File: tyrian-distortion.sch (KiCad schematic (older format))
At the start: 84 parts, among them J1 AudioJack2, J2 AudioJack2, J3 Barrel_Jack_Switch, J4 Conn_01x02_Female, SW1 SW_DPDT_x2, SW2 SW_3PDT, U1 TL072, U2 TL072, U3 TL072, U4 TL072

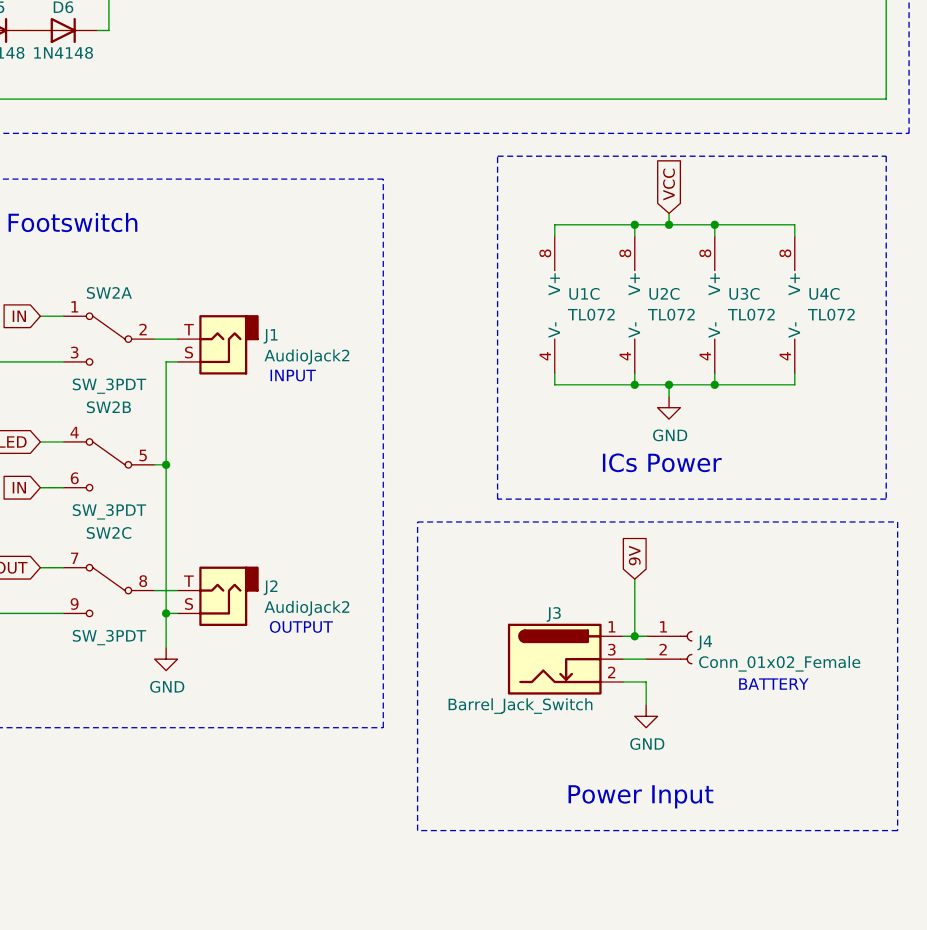
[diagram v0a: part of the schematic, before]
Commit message: feat: Create footprint associations
- Adds custom footprints for DPDT and 3PDT
- Minor fixes to schema
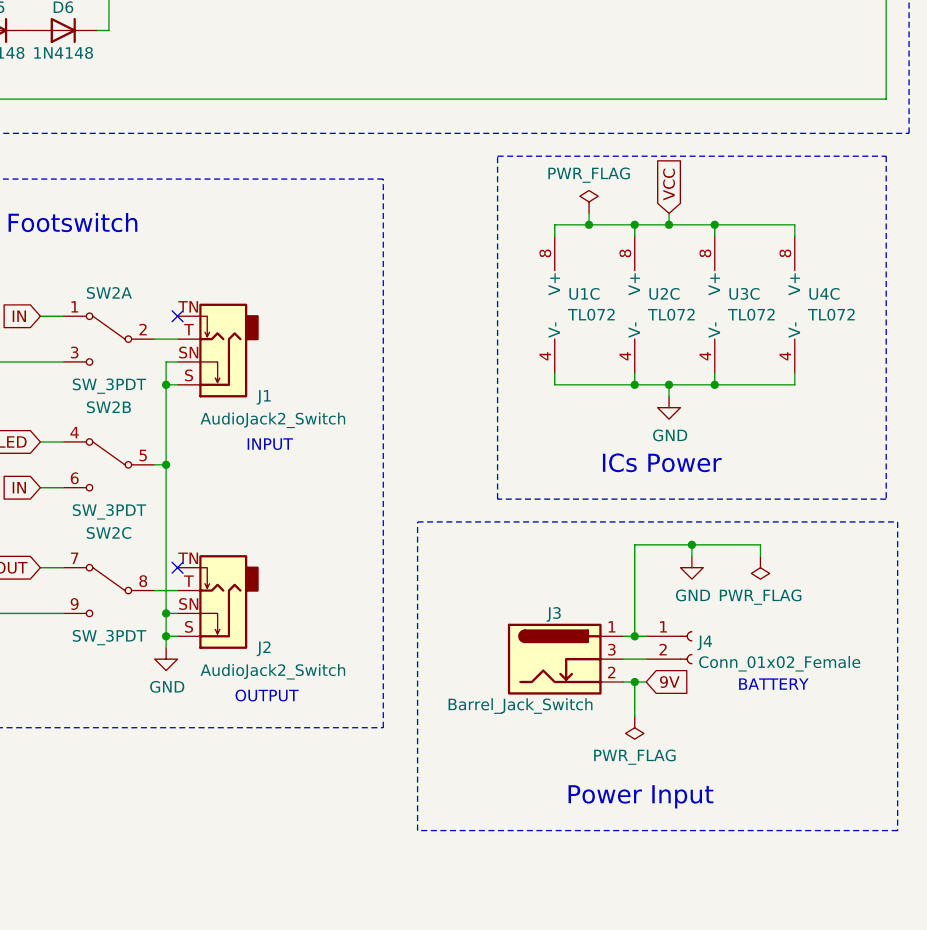
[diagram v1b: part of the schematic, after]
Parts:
- removed J1, J2: AudioJack2, symbol Connector:AudioJack2
- added J1, J2: AudioJack2_Switch, Connector_Audio:Jack_6.35mm_Neutrik_NMJ4HCD2_Horizontal, symbol Connector:AudioJack2_Switch
- C1, C17: footprint (none) -> Capacitor_THT:C_Disc_D5.0mm_W2.5mm_P2.50mm
- C10, C11, C12, C13, C14, C15, C16, C18, C19, C20, C22, C23, C24, C26, C3, C4, C5, C6, C7, C9: footprint (none) -> Capacitor_THT:C_Disc_D3.4mm_W2.1mm_P2.50mm
- C2: footprint (none) -> Capacitor_THT:CP_Radial_D5.0mm_P2.00mm
- C21, C25, C8: footprint (none) -> Capacitor_THT:C_Disc_D8.0mm_W2.5mm_P5.00mm
- D2: footprint (none) -> LED_THT:LED_D5.0mm
- D7, D8: footprint (none) -> LED_THT:LED_D3.0mm
- J3: footprint (none) -> Connector_BarrelJack:BarrelJack_Wuerth_6941xx301002
- J4: footprint (none) -> tyrian-distortion:TerminalBlock_2pin_2.54mm
- R1, R10, R11, R12, R13, R14, R15, R16, R17, R18, R19, R2, R20, R21, R22, R23, R24, R25, R26, R27, R28, R29, R3, R30, R31, R32, R33, R34, R35, R4, R5, R6, R7, R8, R9: footprint (none) -> Resistor_THT:R_Axial_DIN0207_L6.3mm_D2.5mm_P10.16mm_Horizontal
- RV1, RV2, RV3, RV4, RV5: footprint (none) -> tyrian-distortion:Tayda_Potentiometer
- SW1: footprint (none) -> tyrian-distortion:DPDT_Toggle_Switch
- SW2: footprint (none) -> tyrian-distortion:3PDT_Toggle_Switch
- U1, U2, U3, U4: footprint (none) -> Package_DIP:DIP-8_W7.62mm
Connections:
- net 9V: now also J3.2; no longer J3.1, J4.1 (Pin_1)
- net GND: now also J3.1, J4.1 (Pin_1), J1.S, J1.SN, J2.S, J2.SN; no longer J3.2
- net at SW2.2: now also J1.T
- net at SW2.8: now also J2.T
- no-connect marks 0 -> 2
